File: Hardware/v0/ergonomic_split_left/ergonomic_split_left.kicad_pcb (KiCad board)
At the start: 2 copper layers, 189.3 x 173.4 mm, 95 parts, among them J1 USB_C_Receptacle_USB2.0, J5 Conn_02x03_Odd_Even, SW1 SW_Push, SW10 L31, SW11 L41, SW12 L51, SW13 L02, SW14 L12, SW15 L22, SW16 L32, SW17 L42, SW18 L52, SW19 L03, SW2 L00, SW20 L13, SW21 L23, SW22 L33, SW23 L43, SW24 L53, SW25 L04, SW26 L14, SW27 L24, SW28 L34, SW29 L44, SW3 L10, SW30 L54, SW31 L05, SW32 L15, SW33 L25, SW34 L35, SW35 L55, SW36 L16, SW37 L36, SW38 L56, SW39 L06, SW4 L20, SW40 L_Encoder, SW5 L30, SW6 L40, SW7 L01, SW8 L11, SW9 L21, U1 SRV05-4, U2 PCAL9555AHF, U6 ATmega32U4-AU, U9 TCR2EF33, X2 KC2016K

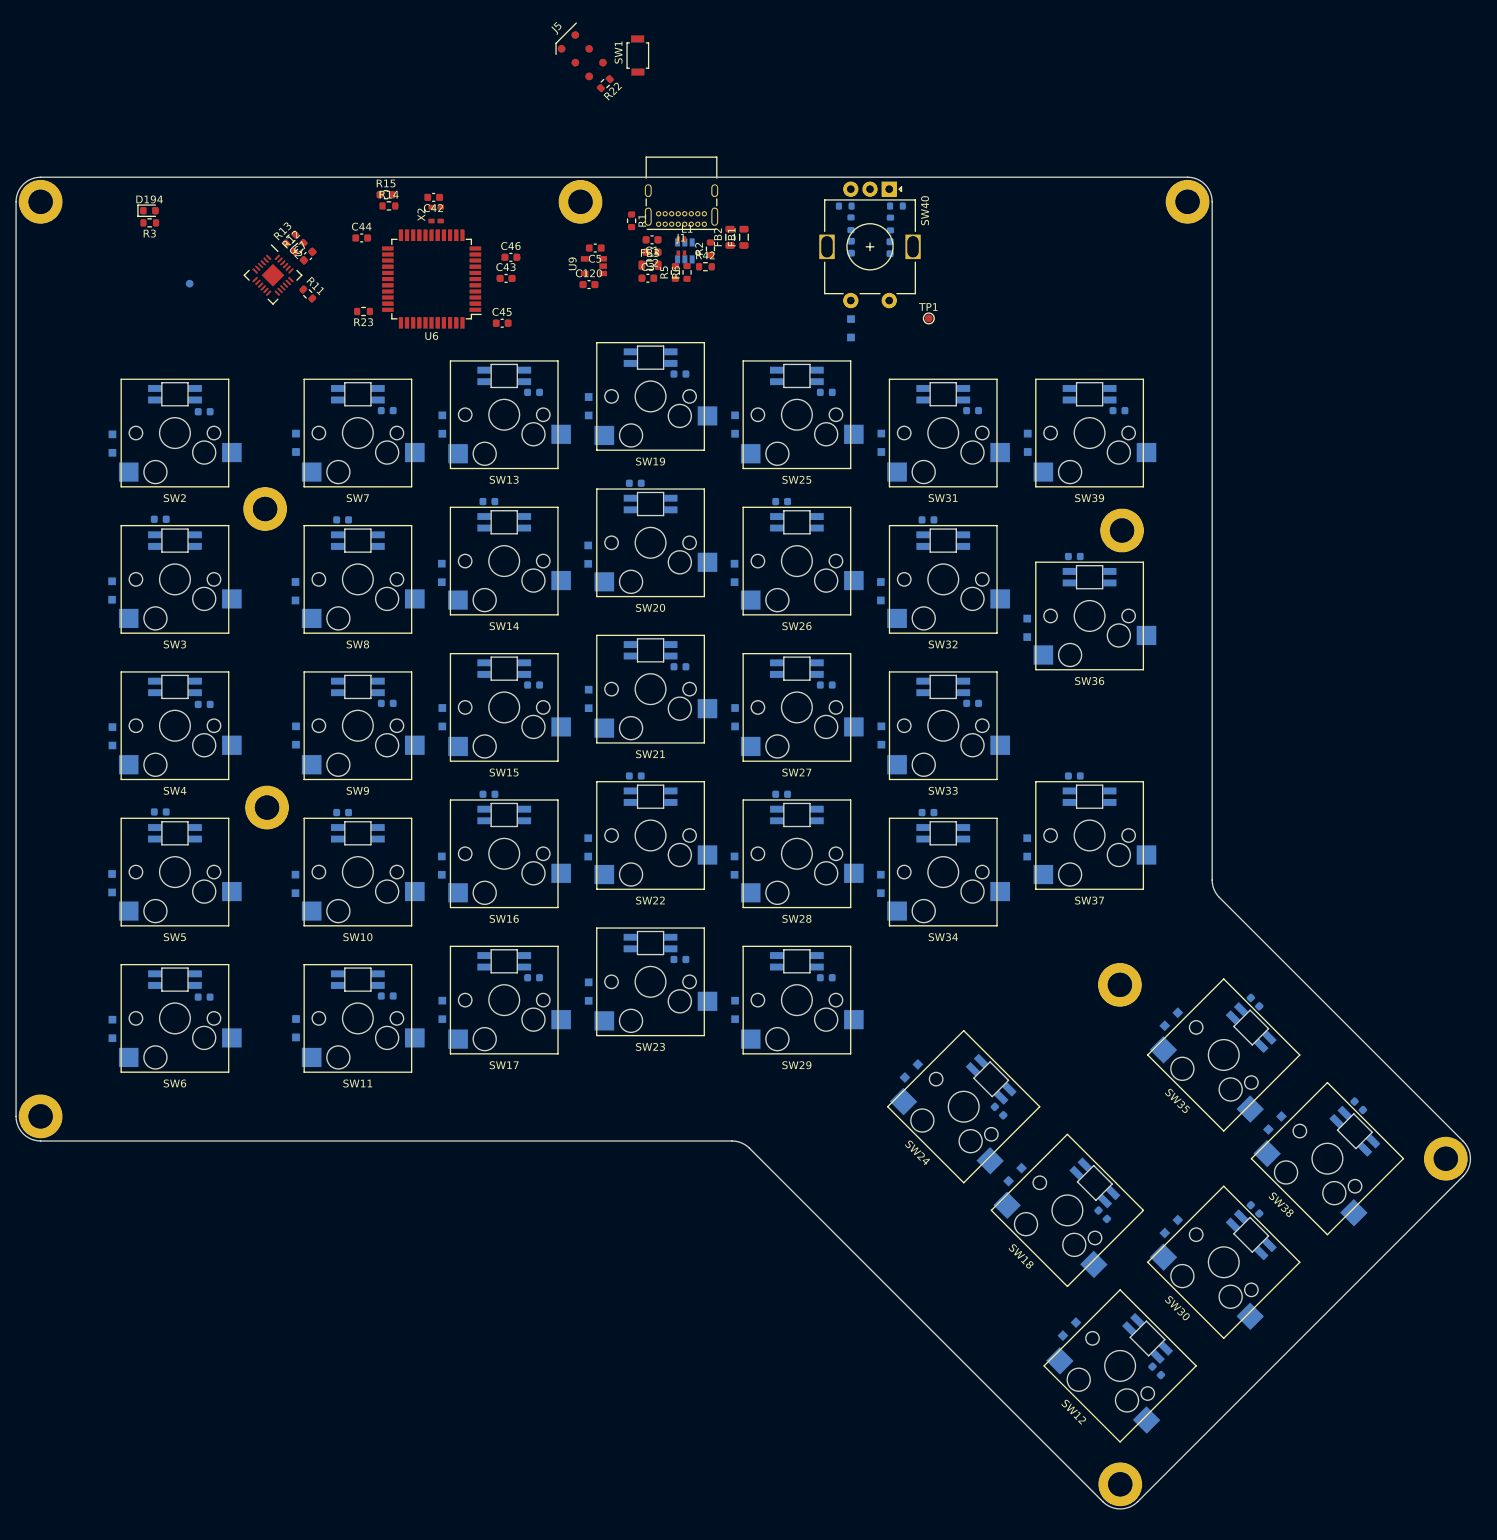
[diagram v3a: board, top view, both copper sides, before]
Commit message: Adding power and ground planes Adding right interface USB C connector Pin swapping on ATMEGA
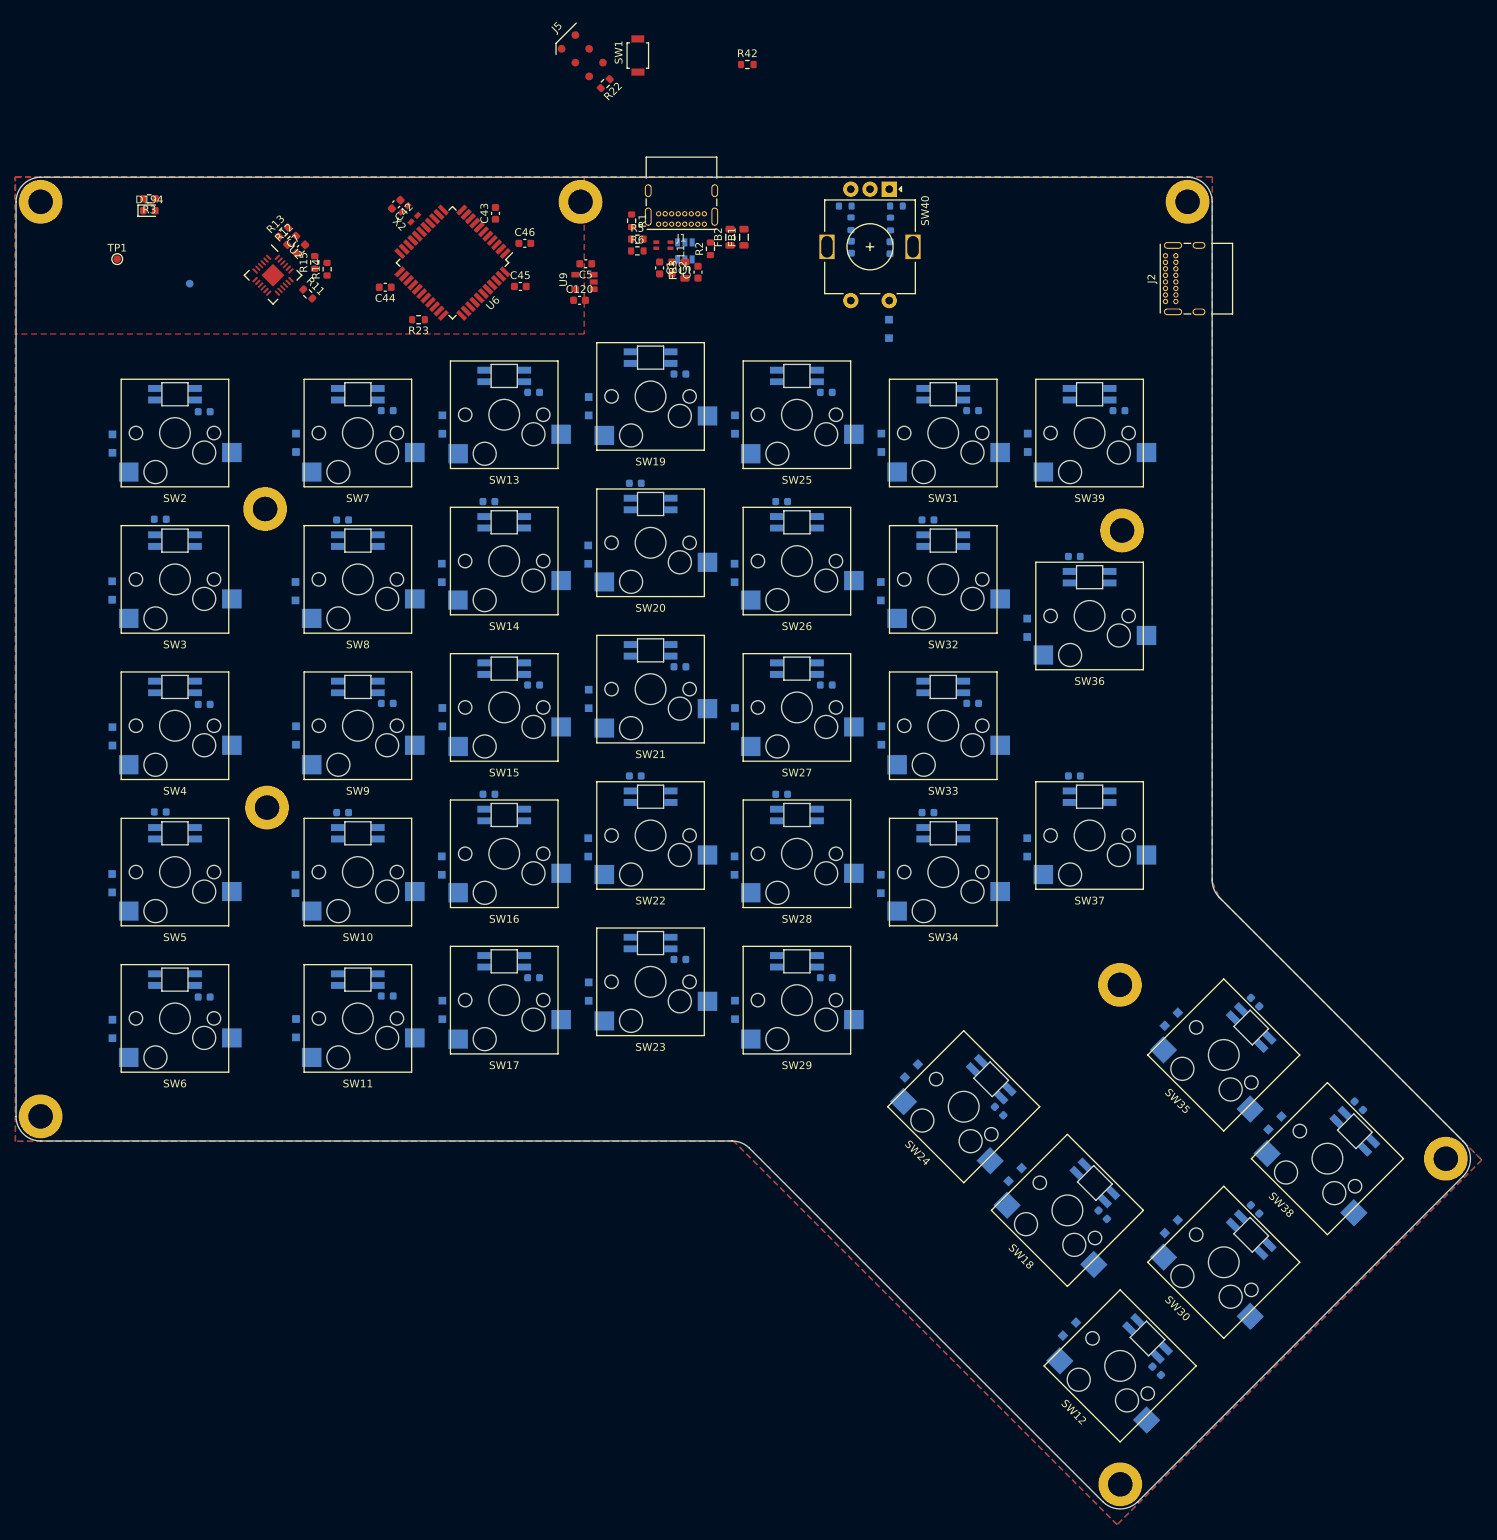
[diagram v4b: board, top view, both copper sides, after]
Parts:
- added J2: USB_C_Receptical_USB4085, Connector_USB:USB_C_Receptacle_GCT_USB4085, F.Cu at (222.6, 71.8)
- moved TP1 105.9 mm to (86.1, 66.3)
- moved R42 26.9 mm to (168.2, 40.9)
- moved R15 12.8 mm to (111.9, 66.7), turned to 90 degrees
- moved R14 11.5 mm to (113.5, 67.6), turned to 90 degrees
- moved C43 8.58 mm to (135.4, 60.3), turned to 90 degrees
- moved R23 7.23 mm to (125.4, 74.1)
- moved C44 7.11 mm to (121.0, 69.9), turned to 180 degrees
- moved R6 7.05 mm to (153.9, 65.2), turned to 0 degrees
- moved C3 6.58 mm to (161.7, 68.0), turned to 90 degrees
- moved R5 6.57 mm to (153.9, 63.7), turned to 0 degrees
- moved C45 5.33 mm to (138.6, 69.8)
- moved C42 4.96 mm to (122.5, 59.1), turned to 225 degrees
- moved D1 4.94 mm to (186.6, 76.5)
- moved FB3 4.60 mm to (160.0, 67.7), turned to 90 degrees
- moved C1 3.79 mm to (156.7, 67.4), turned to 270 degrees
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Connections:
- D1 pad 1: /IO Expander/ROW[6] -> /IO Expander/COL[6]
- SW40 pad S1: Net-(D1-Pad2) -> /IO Expander/ROW[6]
- SW40 pad S2: /IO Expander/COL[6] -> Net-(D1-Pad2)
- U6 pad 12: Net-(U6-Pad12) -> /uController/nCAPS_LED
- U6 pad 22: /uController/nCAPS_LED -> Net-(U6-Pad22)
- U6 pad 26: /Switch Matrix/ENCODER_A_L -> Net-(U6-Pad26)
- U6 pad 27: /Switch Matrix/ENCODER_B_L -> Net-(U6-Pad27)
- U6 pad 38: /Right Interface/ENCODER_B_R -> /Switch Matrix/ENCODER_B_L
- U6 pad 39: /Right Interface/ENCODER_A_R -> /Switch Matrix/ENCODER_A_L
- U6 pad 40: Net-(U6-Pad40) -> /Right Interface/ENCODER_B_R
- U6 pad 41: Net-(U6-Pad41) -> /Right Interface/ENCODER_A_R
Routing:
- added copper zone on F.Cu, net +3V3
- added copper zone on F.Cu, net +5V
- added copper zone on B.Cu, net GND

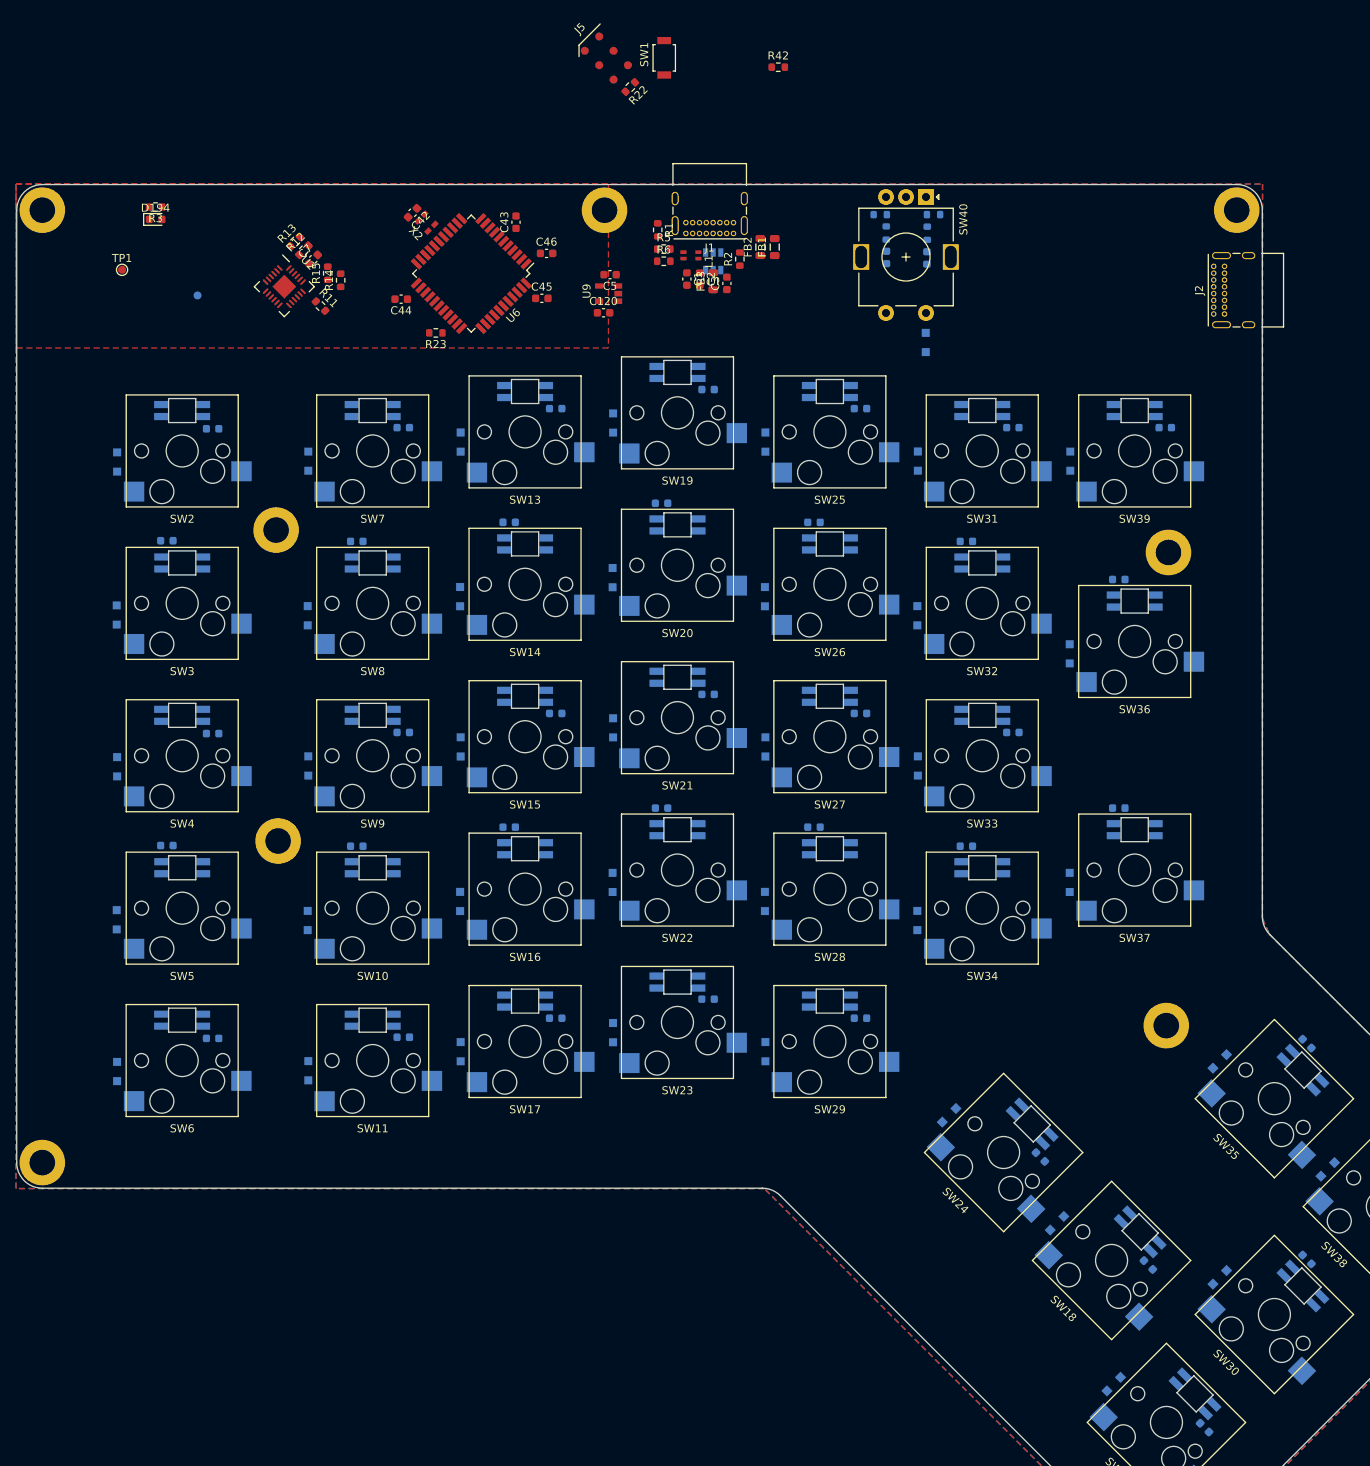
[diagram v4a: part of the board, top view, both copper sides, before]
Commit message: Debug connectors Adding I2C debug header Changed SPI programming header to edge mount Changed right interface connector to IDC Cleaning up schematic
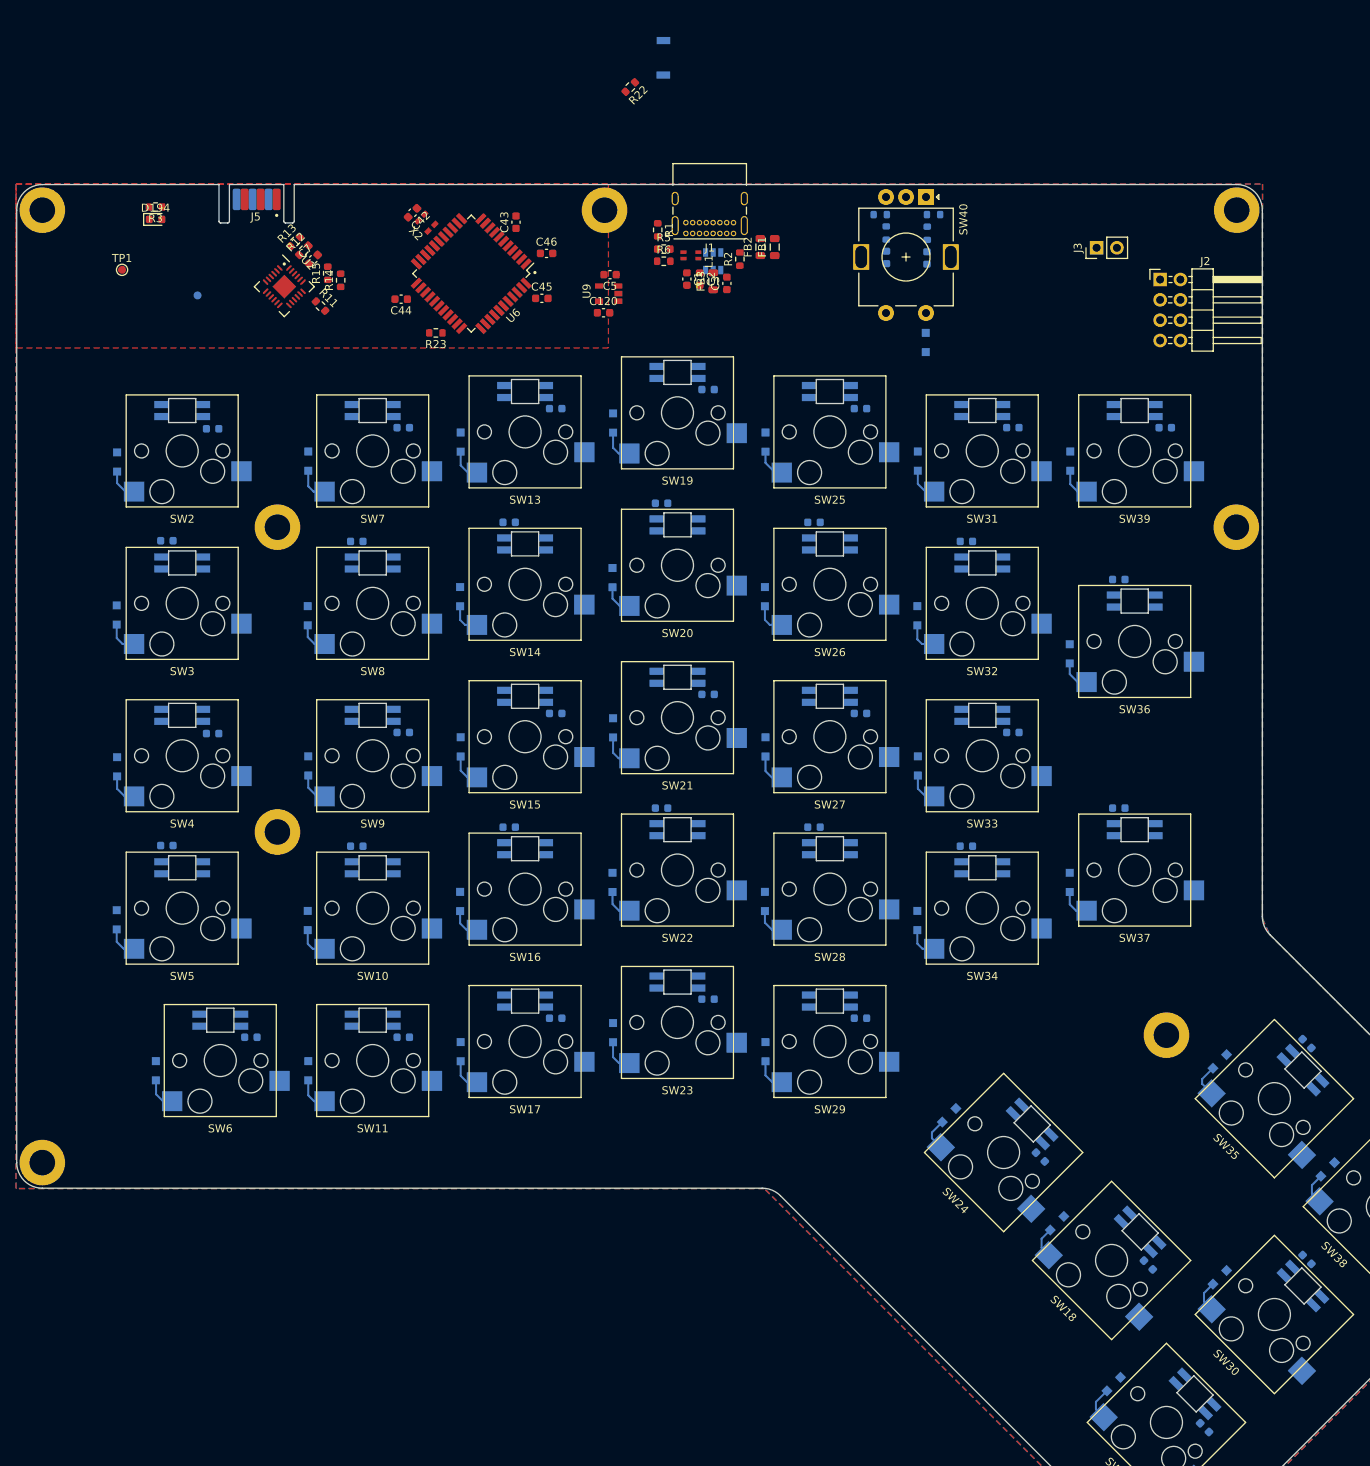
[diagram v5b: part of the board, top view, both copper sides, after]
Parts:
- removed R42: 1K5, resistor_smd:R_0603_1608Metric
- added J3: Conn_01x02_Male, Connector_PinHeader_2.54mm:PinHeader_1x02_P2.54mm_Vertical, F.Cu at (208.0, 63.5)
- J2: value USB_C_Receptical_USB4085 -> Right_Interface; footprint Connector_USB:USB_C_Receptacle_GCT_USB4085 -> Connector_PinHeader_2.54mm:PinHeader_2x04_P2.54mm_Horizontal
- J5: footprint custom_footprint_library:ISP_POGO -> custom_footprint_library:Conn_AVX_PCB_Edge_02x03
- SW1: moved to B.Cu
- SW6: footprint custom_footprint_library:CherryMX_1.50u_KailhSocket_Integrated_Reversed -> custom_footprint_library:CherryMX_1.00u_KailhSocket_Integrated_Reversed
- moved J5 42.8 mm to (105.5, 57.4), turned to 180 degrees
- moved H9 9.05 mm to (225.4, 98.4)
- moved J2 7.96 mm to (215.9, 67.5), turned to 0 degrees
- moved SW6 4.77 mm to (98.4, 165.1)
- moved H10 1.20 mm to (216.7, 161.9)
- moved H4 1.13 mm to (105.6, 136.5)
- moved H7 0.40 mm to (105.6, 98.4)
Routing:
- net Net-(SW12-Pad2): track 0.00 -> 4.26 mm
- net Net-(SW7-Pad2): track 0.00 -> 4.26 mm
- net Net-(SW21-Pad2): track 0.00 -> 4.24 mm
- net Net-(SW19-Pad2): track 0.00 -> 4.23 mm
- net Net-(SW11-Pad2): track 0.00 -> 4.22 mm
- net Net-(SW23-Pad2): track 0.00 -> 4.21 mm
- net Net-(SW35-Pad2): track 0.00 -> 4.19 mm
- net Net-(SW27-Pad2): track 0.00 -> 4.18 mm
- net Net-(SW17-Pad2): track 0.00 -> 4.18 mm
- net Net-(SW3-Pad2): track 0.00 -> 4.17 mm
- net Net-(SW15-Pad2): track 0.00 -> 4.15 mm
- net Net-(SW29-Pad2): track 0.00 -> 4.15 mm
- net Net-(SW24-Pad2): track 0.00 -> 4.14 mm
- net Net-(SW6-Pad2): track 0.00 -> 4.13 mm
- net Net-(SW13-Pad2): track 0.00 -> 4.12 mm
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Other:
- outline, holes or cut-outs redrawn
